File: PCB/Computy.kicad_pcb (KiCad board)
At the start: 2 copper layers, 50 x 100 mm, 59 parts, among them J1 USB_C_Receptacle_USB2.0_16P, J2 Conn_ARM_JTAG_SWD_10, J3 Conn_01x03_Socket, J4 Conn_01x04_Socket, J5 Conn_01x04_Socket, J6 Conn_01x05, J7 Conn_01x05, J8 Conn_01x04_Socket, M1 Motor_Servo, M2 Motor_Servo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

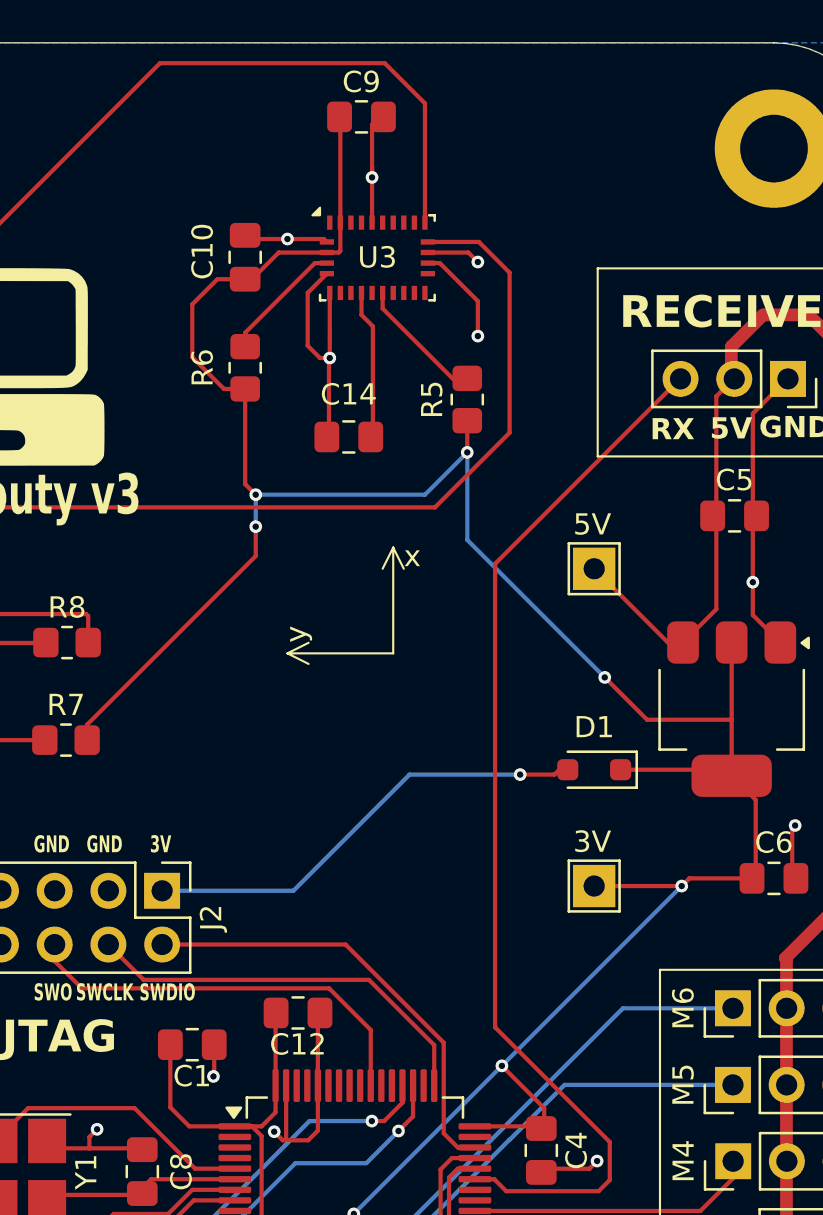
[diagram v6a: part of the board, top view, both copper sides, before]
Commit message: Expose UART5 and I2C2 on the PCB
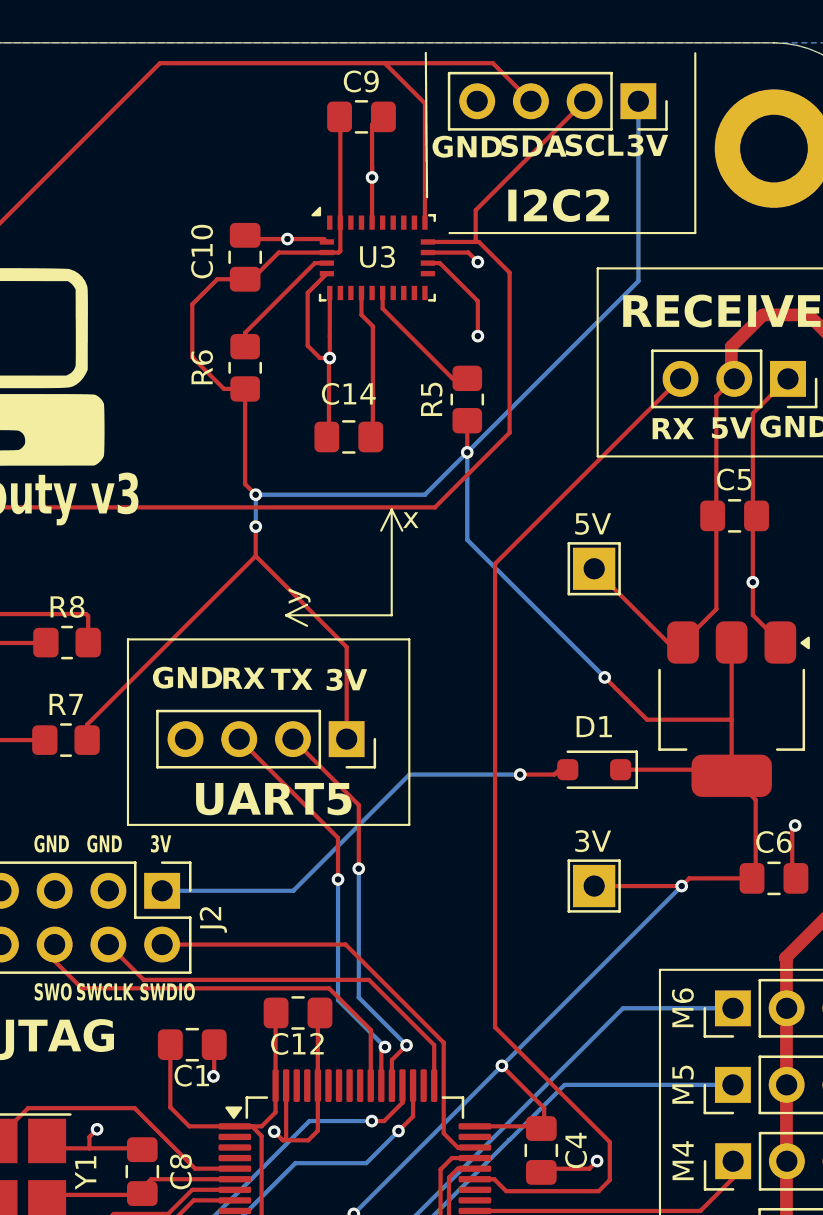
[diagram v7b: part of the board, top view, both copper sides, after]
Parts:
- added J10: Conn_01x04_Socket, Connector_PinSocket_2.54mm:PinSocket_1x04_P2.54mm_Vertical, F.Cu at (109.8, 73.1)
- added J9: Conn_01x04_Socket, Connector_PinSocket_2.54mm:PinSocket_1x04_P2.54mm_Vertical, F.Cu at (123.6, 42.9)
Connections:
- U1 pad 53: unconnected-(U1-PC12-Pad53) -> /UART5_TX
- U1 pad 54: unconnected-(U1-PD2-Pad54) -> /UART5_RX
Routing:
- net +3.3V: track 259.9 -> 290.3 mm
- net /UART5_RX: track 0.00 -> 19.3 mm, vias 0 -> 2
- net /UART5_TX: track 0.00 -> 18.9 mm, vias 0 -> 2
- net /I2C2_SCL: track 118.6 -> 127.4 mm
- net /I2C2_SDA: track 131.2 -> 138.8 mm
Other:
- board text added: "I2C2"
- board text added: "UART5"
